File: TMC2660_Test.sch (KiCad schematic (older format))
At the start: 50 parts, among them P101 CONN_4, P102 CONN_4, P103 CONN_2, P104 CONN_13X2, P105 CONN_4, P106 CONN_4, U101 TMC2660, U102 TMC2660, U103 TMC2660, U104 TMC2660

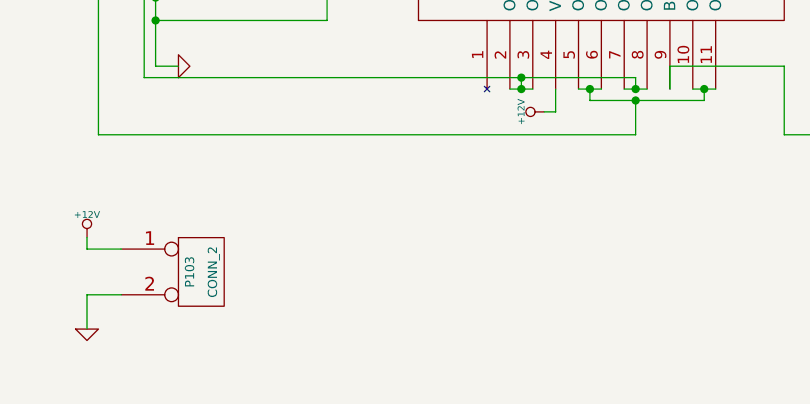
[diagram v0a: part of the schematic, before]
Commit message: Add mounting holes, dummy.
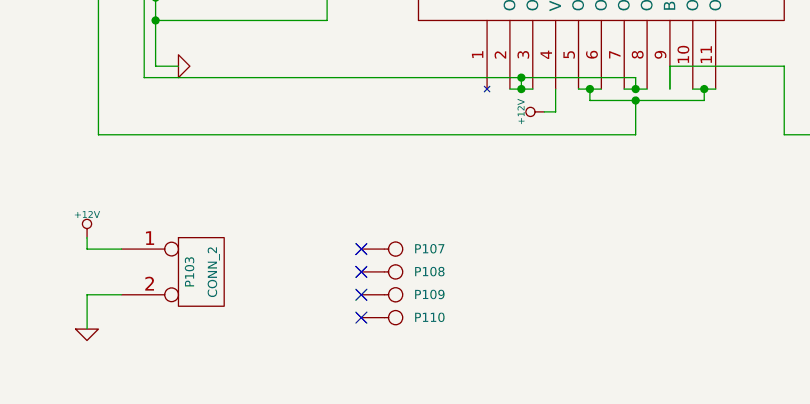
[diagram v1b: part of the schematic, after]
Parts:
- added P107, P108, P109, P110: CONN_1, symbol CONN_1
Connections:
- no-connect marks 8 -> 12
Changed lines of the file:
@@
 $EndComp
 $Comp
-L GND #PWR01
+L GND #PWR103
 U 1 1 53402B12
 P 1500 3100
-F 0 "#PWR01" H 1500 3100 30  0001 C CNN
+F 0 "#PWR103" H 1500 3100 30  0001 C CNN
 F 1 "GND" H 1500 3030 30  0001 C CNN
 F 2 "" H 1500 3100 60  0000 C CNN
@@
 $EndComp
 $Comp
-L VCC #PWR02
+L VCC #PWR107
 U 1 1 53402B23
 P 1750 2200
-F 0 "#PWR02" H 1750 2300 30  0001 C CNN
+F 0 "#PWR107" H 1750 2300 30  0001 C CNN
 F 1 "VCC" H 1750 2300 30  0000 C CNN
 F 2 "" H 1750 2200 60  0000 C CNN
@@
 $EndComp
 $Comp
-L +12V #PWR03
+L +12V #PWR105
 U 1 1 53402B52
 P 1650 1700
-F 0 "#PWR03" H 1650 1650 20  0001 C CNN
+F 0 "#PWR105" H 1650 1650 20  0001 C CNN
 F 1 "+12V" H 1650 1800 30  0000 C CNN
 F 2 "" H 1650 1700 60  0000 C CNN
@@
 X-STEP
 $Comp
-L +12V #PWR04
+L +12V #PWR110
 U 1 1 53402CCE
 P 3100 3300
-F 0 "#PWR04" H 3100 3250 20  0001 C CNN
+F 0 "#PWR110" H 3100 3250 20  0001 C CNN
 F 1 "+12V" H 3100 3400 30  0000 C CNN
 F 2 "" H 3100 3300 60  0000 C CNN
@@
 $EndComp
 $Comp
-L +12V #PWR05
+L +12V #PWR109
 U 1 1 53402EAB
 P 3100 900
-F 0 "#PWR05" H 3100 850 20  0001 C CNN
+F 0 "#PWR109" H 3100 850 20  0001 C CNN
 F 1 "+12V" H 3100 1000 30  0000 C CNN
 F 2 "" H 3100 900 60  0000 C CNN
@@
 	4450 1900 4600 1900
 $Comp
-L GND #PWR06
+L GND #PWR113
 U 1 1 5340331C
 P 5350 2300
-F 0 "#PWR06" H 5350 2300 30  0001 C CNN
+F 0 "#PWR113" H 5350 2300 30  0001 C CNN
 F 1 "GND" H 5350 2230 30  0001 C CNN
 F 2 "" H 5350 2300 60  0000 C CNN
@@
 $EndComp
 $Comp
-L GND #PWR07
+L GND #PWR104
 U 1 1 5340488D
 P 1500 6200
-F 0 "#PWR07" H 1500 6200 30  0001 C CNN
+F 0 "#PWR104" H 1500 6200 30  0001 C CNN
 F 1 "GND" H 1500 6130 30  0001 C CNN
 F 2 "" H 1500 6200 60  0000 C CNN
@@
 $EndComp
 $Comp
-L VCC #PWR08
+L VCC #PWR108
 U 1 1 53404893
 P 1750 5300
-F 0 "#PWR08" H 1750 5400 30  0001 C CNN
+F 0 "#PWR108" H 1750 5400 30  0001 C CNN
 F 1 "VCC" H 1750 5400 30  0000 C CNN
 F 2 "" H 1750 5300 60  0000 C CNN
@@
 $EndComp
 $Comp
-L +12V #PWR09
+L +12V #PWR106
 U 1 1 53404899
 P 1650 4800
-F 0 "#PWR09" H 1650 4750 20  0001 C CNN
+F 0 "#PWR106" H 1650 4750 20  0001 C CNN
 F 1 "+12V" H 1650 4900 30  0000 C CNN
 F 2 "" H 1650 4800 60  0000 C CNN
@@
 Z-STEP
 $Comp
-L +12V #PWR010
+L +12V #PWR112
 U 1 1 534048B5
 P 3100 6400
-F 0 "#PWR010" H 3100 6350 20  0001 C CNN
+F 0 "#PWR112" H 3100 6350 20  0001 C CNN
 F 1 "+12V" H 3100 6500 30  0000 C CNN
 F 2 "" H 3100 6400 60  0000 C CNN
@@
 $EndComp
 $Comp
-L +12V #PWR011
+L +12V #PWR111
 U 1 1 534048BB
 P 3100 4000
-F 0 "#PWR011" H 3100 3950 20  0001 C CNN
+F 0 "#PWR111" H 3100 3950 20  0001 C CNN
 F 1 "+12V" H 3100 4100 30  0000 C CNN
 F 2 "" H 3100 4000 60  0000 C CNN
@@
 	4450 5000 4600 5000
 $Comp
-L GND #PWR012
+L GND #PWR114
 U 1 1 53404906
 P 5350 5400
-F 0 "#PWR012" H 5350 5400 30  0001 C CNN
+F 0 "#PWR114" H 5350 5400 30  0001 C CNN
 F 1 "GND" H 5350 5330 30  0001 C CNN
 F 2 "" H 5350 5400 60  0000 C CNN
@@
 $EndComp
 $Comp
-L GND #PWR013
+L GND #PWR117
 U 1 1 53404974
 P 6950 3100
-F 0 "#PWR013" H 6950 3100 30  0001 C CNN
+F 0 "#PWR117" H 6950 3100 30  0001 C CNN
 F 1 "GND" H 6950 3030 30  0001 C CNN
 F 2 "" H 6950 3100 60  0000 C CNN
@@
 $EndComp
 $Comp
-L VCC #PWR014
+L VCC #PWR120
 U 1 1 5340497A
 P 7200 2200
-F 0 "#PWR014" H 7200 2300 30  0001 C CNN
+F 0 "#PWR120" H 7200 2300 30  0001 C CNN
 F 1 "VCC" H 7200 2300 30  0000 C CNN
 F 2 "" H 7200 2200 60  0000 C CNN
@@
 $EndComp
 $Comp
-L +12V #PWR015
+L +12V #PWR118
 U 1 1 53404980
 P 7100 1700
-F 0 "#PWR015" H 7100 1650 20  0001 C CNN
+F 0 "#PWR118" H 7100 1650 20  0001 C CNN
 F 1 "+12V" H 7100 1800 30  0000 C CNN
 F 2 "" H 7100 1700 60  0000 C CNN
@@
 Y-STEP
 $Comp
-L +12V #PWR016
+L +12V #PWR124
 U 1 1 5340499C
 P 8550 3300
-F 0 "#PWR016" H 8550 3250 20  0001 C CNN
+F 0 "#PWR124" H 8550 3250 20  0001 C CNN
 F 1 "+12V" H 8550 3400 30  0000 C CNN
 F 2 "" H 8550 3300 60  0000 C CNN
@@
 $EndComp
 $Comp
-L +12V #PWR017
+L +12V #PWR123
 U 1 1 534049A2
 P 8550 900
-F 0 "#PWR017" H 8550 850 20  0001 C CNN
+F 0 "#PWR123" H 8550 850 20  0001 C CNN
 F 1 "+12V" H 8550 1000 30  0000 C CNN
 F 2 "" H 8550 900 60  0000 C CNN
@@
 	9900 1900 10050 1900
 $Comp
-L GND #PWR018
+L GND #PWR127
 U 1 1 534049ED
 P 10800 2300
-F 0 "#PWR018" H 10800 2300 30  0001 C CNN
+F 0 "#PWR127" H 10800 2300 30  0001 C CNN
 F 1 "GND" H 10800 2230 30  0001 C CNN
 F 2 "" H 10800 2300 60  0000 C CNN
@@
 $EndComp
 $Comp
-L GND #PWR019
+L GND #PWR119
 U 1 1 53404A5B
 P 7100 6200
-F 0 "#PWR019" H 7100 6200 30  0001 C CNN
+F 0 "#PWR119" H 7100 6200 30  0001 C CNN
 F 1 "GND" H 7100 6130 30  0001 C CNN
 F 2 "" H 7100 6200 60  0000 C CNN
@@
 $EndComp
 $Comp
-L VCC #PWR020
+L VCC #PWR122
 U 1 1 53404A61
 P 7350 5300
-F 0 "#PWR020" H 7350 5400 30  0001 C CNN
+F 0 "#PWR122" H 7350 5400 30  0001 C CNN
 F 1 "VCC" H 7350 5400 30  0000 C CNN
 F 2 "" H 7350 5300 60  0000 C CNN
@@
 $EndComp
 $Comp
-L +12V #PWR021
+L +12V #PWR121
 U 1 1 53404A67
 P 7250 4800
-F 0 "#PWR021" H 7250 4750 20  0001 C CNN
+F 0 "#PWR121" H 7250 4750 20  0001 C CNN
 F 1 "+12V" H 7250 4900 30  0000 C CNN
 F 2 "" H 7250 4800 60  0000 C CNN
@@
 E-STEP
 $Comp
-L +12V #PWR022
+L +12V #PWR126
 U 1 1 53404A83
 P 8700 6400
-F 0 "#PWR022" H 8700 6350 20  0001 C CNN
+F 0 "#PWR126" H 8700 6350 20  0001 C CNN
 F 1 "+12V" H 8700 6500 30  0000 C CNN
 F 2 "" H 8700 6400 60  0000 C CNN
@@
 $EndComp
 $Comp
-L +12V #PWR023
+L +12V #PWR125
 U 1 1 53404A89
 P 8700 4000
-F 0 "#PWR023" H 8700 3950 20  0001 C CNN
+F 0 "#PWR125" H 8700 3950 20  0001 C CNN
 F 1 "+12V" H 8700 4100 30  0000 C CNN
 F 2 "" H 8700 4000 60  0000 C CNN
@@
 	10050 5000 10200 5000
 $Comp
-L GND #PWR024
+L GND #PWR128
 U 1 1 53404AD4
 P 10950 5400
-F 0 "#PWR024" H 10950 5400 30  0001 C CNN
+F 0 "#PWR128" H 10950 5400 30  0001 C CNN
 F 1 "GND" H 10950 5330 30  0001 C CNN
 F 2 "" H 10950 5400 60  0000 C CNN
@@
 $EndComp
 $Comp
-L +12V #PWR025
+L +12V #PWR101
 U 1 1 53404C7D
 P 1100 6950
-F 0 "#PWR025" H 1100 6900 20  0001 C CNN
+F 0 "#PWR101" H 1100 6900 20  0001 C CNN
 F 1 "+12V" H 1100 7050 30  0000 C CNN
 F 2 "" H 1100 6950 60  0000 C CNN
@@
 $EndComp
 $Comp
-L GND #PWR026
+L GND #PWR102
 U 1 1 53404C8C
 P 1100 7350
-F 0 "#PWR026" H 1100 7350 30  0001 C CNN
+F 0 "#PWR102" H 1100 7350 30  0001 C CNN
 F 1 "GND" H 1100 7280 30  0001 C CNN
 F 2 "" H 1100 7350 60  0000 C CNN
@@
 	1100 7000 1250 7000
 $Comp
-L VCC #PWR027
+L VCC #PWR115
 U 1 1 5340502F
 P 5500 5800
-F 0 "#PWR027" H 5500 5900 30  0001 C CNN
+F 0 "#PWR115" H 5500 5900 30  0001 C CNN
 F 1 "VCC" H 5500 5900 30  0000 C CNN
 F 2 "" H 5500 5800 60  0000 C CNN
@@
 $EndComp
 $Comp
-L GND #PWR028
+L GND #PWR116
 U 1 1 5340503E
 P 5950 7550
-F 0 "#PWR028" H 5950 7550 30  0001 C CNN
+F 0 "#PWR116" H 5950 7550 30  0001 C CNN
 F 1 "GND" H 5950 7480 30  0001 C CNN
 F 2 "" H 5950 7550 60  0000 C CNN
@@
 Wire Wire Line
 	1150 800  1150 1950
+$Comp
+L CONN_1 P107
+U 1 1 53442419
+P 2450 7000
+F 0 "P107" H 2530 7000 40  0000 L CNN
+F 1 "CONN_1" H 2450 7055 30  0001 C CNN
+F 2 "" H 2450 7000 60  0000 C CNN
+F 3 "" H 2450 7000 60  0000 C CNN
+	1    2450 7000
+	1    0    0    -1
+$EndComp
+$Comp
+L CONN_1 P108
+U 1 1 53442428
+P 2450 7100
+F 0 "P108" H 2530 7100 40  0000 L CNN
+F 1 "CONN_1" H 2450 7155 30  0001 C CNN
+F 2 "" H 2450 7100 60  0000 C CNN
+F 3 "" H 2450 7100 60  0000 C CNN
+	1    2450 7100
+	1    0    0    -1
+$EndComp
+$Comp
+L CONN_1 P109
+U 1 1 53442437
+P 2450 7200
+F 0 "P109" H 2530 7200 40  0000 L CNN
+F 1 "CONN_1" H 2450 7255 30  0001 C CNN
+F 2 "" H 2450 7200 60  0000 C CNN
+F 3 "" H 2450 7200 60  0000 C CNN
+	1    2450 7200
+	1    0    0    -1
+$EndComp
+$Comp
+L CONN_1 P110
+U 1 1 53442446
+P 2450 7300
+F 0 "P110" H 2530 7300 40  0000 L CNN
+F 1 "CONN_1" H 2450 7355 30  0001 C CNN
+F 2 "" H 2450 7300 60  0000 C CNN
+F 3 "" H 2450 7300 60  0000 C CNN
+	1    2450 7300
+	1    0    0    -1
+$EndComp
+NoConn ~ 2300 7000
+NoConn ~ 2300 7100
+NoConn ~ 2300 7200
+NoConn ~ 2300 7300
 $EndSCHEMATC

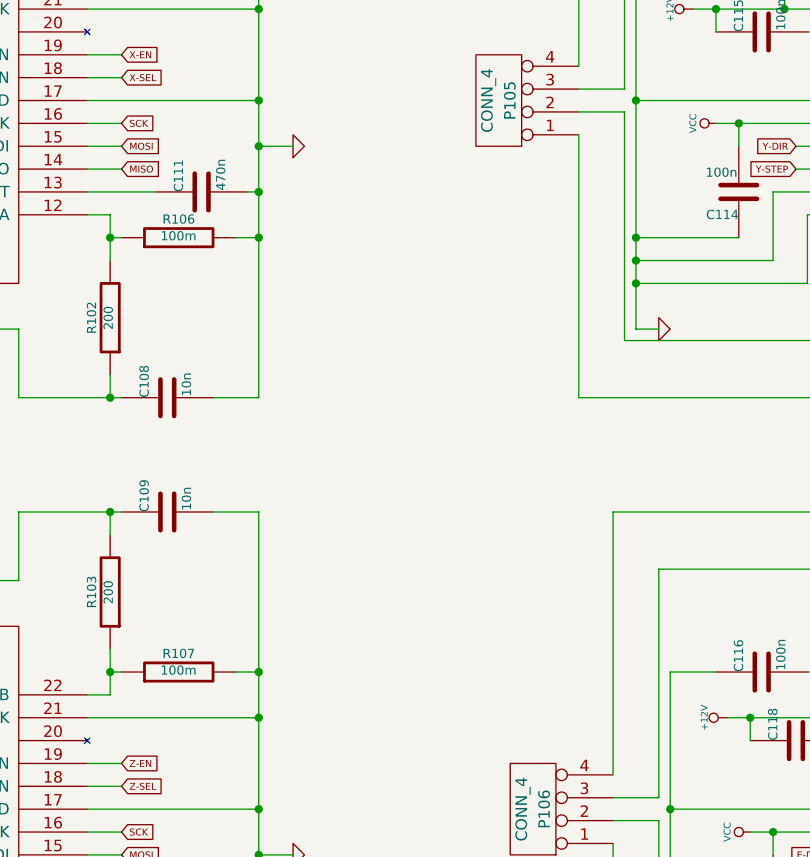
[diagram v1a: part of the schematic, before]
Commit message: Add decoupling caps--one ceramic and one electrolytic per driver.
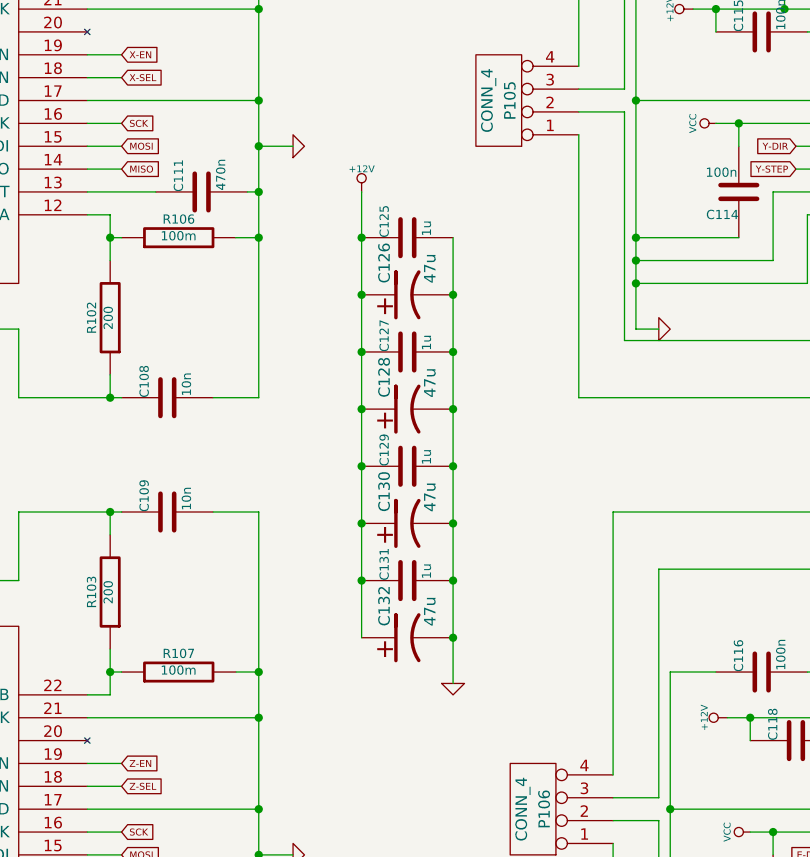
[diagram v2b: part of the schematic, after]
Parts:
- added C125, C127, C129, C131: 1u, symbol C
- added C126, C128, C130, C132: 47u, symbol CP1
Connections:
- net +12V: now also C125.1, C126.1, C127.1, C128.1, C129.1, C130.1, C131.1, C132.1
- net GND: now also C125.2, C126.2, C127.2, C128.2, C129.2, C130.2, C131.2, C132.2
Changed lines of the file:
@@
 $EndComp
 $Comp
-L GND #PWR103
+L GND #PWR01
 U 1 1 53402B12
 P 1500 3100
-F 0 "#PWR103" H 1500 3100 30  0001 C CNN
+F 0 "#PWR01" H 1500 3100 30  0001 C CNN
 F 1 "GND" H 1500 3030 30  0001 C CNN
 F 2 "" H 1500 3100 60  0000 C CNN
@@
 $EndComp
 $Comp
-L VCC #PWR107
+L VCC #PWR02
 U 1 1 53402B23
 P 1750 2200
-F 0 "#PWR107" H 1750 2300 30  0001 C CNN
+F 0 "#PWR02" H 1750 2300 30  0001 C CNN
 F 1 "VCC" H 1750 2300 30  0000 C CNN
 F 2 "" H 1750 2200 60  0000 C CNN
@@
 $EndComp
 $Comp
-L +12V #PWR105
+L +12V #PWR03
 U 1 1 53402B52
 P 1650 1700
-F 0 "#PWR105" H 1650 1650 20  0001 C CNN
+F 0 "#PWR03" H 1650 1650 20  0001 C CNN
 F 1 "+12V" H 1650 1800 30  0000 C CNN
 F 2 "" H 1650 1700 60  0000 C CNN
@@
 X-STEP
 $Comp
-L +12V #PWR110
+L +12V #PWR04
 U 1 1 53402CCE
 P 3100 3300
-F 0 "#PWR110" H 3100 3250 20  0001 C CNN
+F 0 "#PWR04" H 3100 3250 20  0001 C CNN
 F 1 "+12V" H 3100 3400 30  0000 C CNN
 F 2 "" H 3100 3300 60  0000 C CNN
@@
 $EndComp
 $Comp
-L +12V #PWR109
+L +12V #PWR05
 U 1 1 53402EAB
 P 3100 900
-F 0 "#PWR109" H 3100 850 20  0001 C CNN
+F 0 "#PWR05" H 3100 850 20  0001 C CNN
 F 1 "+12V" H 3100 1000 30  0000 C CNN
 F 2 "" H 3100 900 60  0000 C CNN
@@
 	4450 1900 4600 1900
 $Comp
-L GND #PWR113
+L GND #PWR06
 U 1 1 5340331C
 P 5350 2300
-F 0 "#PWR113" H 5350 2300 30  0001 C CNN
+F 0 "#PWR06" H 5350 2300 30  0001 C CNN
 F 1 "GND" H 5350 2230 30  0001 C CNN
 F 2 "" H 5350 2300 60  0000 C CNN
@@
 $EndComp
 $Comp
-L GND #PWR104
+L GND #PWR07
 U 1 1 5340488D
 P 1500 6200
-F 0 "#PWR104" H 1500 6200 30  0001 C CNN
+F 0 "#PWR07" H 1500 6200 30  0001 C CNN
 F 1 "GND" H 1500 6130 30  0001 C CNN
 F 2 "" H 1500 6200 60  0000 C CNN
@@
 $EndComp
 $Comp
-L VCC #PWR108
+L VCC #PWR08
 U 1 1 53404893
 P 1750 5300
-F 0 "#PWR108" H 1750 5400 30  0001 C CNN
+F 0 "#PWR08" H 1750 5400 30  0001 C CNN
 F 1 "VCC" H 1750 5400 30  0000 C CNN
 F 2 "" H 1750 5300 60  0000 C CNN
@@
 $EndComp
 $Comp
-L +12V #PWR106
+L +12V #PWR09
 U 1 1 53404899
 P 1650 4800
-F 0 "#PWR106" H 1650 4750 20  0001 C CNN
+F 0 "#PWR09" H 1650 4750 20  0001 C CNN
 F 1 "+12V" H 1650 4900 30  0000 C CNN
 F 2 "" H 1650 4800 60  0000 C CNN
@@
 Z-STEP
 $Comp
-L +12V #PWR112
+L +12V #PWR010
 U 1 1 534048B5
 P 3100 6400
-F 0 "#PWR112" H 3100 6350 20  0001 C CNN
+F 0 "#PWR010" H 3100 6350 20  0001 C CNN
 F 1 "+12V" H 3100 6500 30  0000 C CNN
 F 2 "" H 3100 6400 60  0000 C CNN
@@
 $EndComp
 $Comp
-L +12V #PWR111
+L +12V #PWR011
 U 1 1 534048BB
 P 3100 4000
-F 0 "#PWR111" H 3100 3950 20  0001 C CNN
+F 0 "#PWR011" H 3100 3950 20  0001 C CNN
 F 1 "+12V" H 3100 4100 30  0000 C CNN
 F 2 "" H 3100 4000 60  0000 C CNN
@@
 	4450 5000 4600 5000
 $Comp
-L GND #PWR114
+L GND #PWR012
 U 1 1 53404906
 P 5350 5400
-F 0 "#PWR114" H 5350 5400 30  0001 C CNN
+F 0 "#PWR012" H 5350 5400 30  0001 C CNN
 F 1 "GND" H 5350 5330 30  0001 C CNN
 F 2 "" H 5350 5400 60  0000 C CNN
@@
 $EndComp
 $Comp
-L GND #PWR117
+L GND #PWR013
 U 1 1 53404974
 P 6950 3100
-F 0 "#PWR117" H 6950 3100 30  0001 C CNN
+F 0 "#PWR013" H 6950 3100 30  0001 C CNN
 F 1 "GND" H 6950 3030 30  0001 C CNN
 F 2 "" H 6950 3100 60  0000 C CNN
@@
 $EndComp
 $Comp
-L VCC #PWR120
+L VCC #PWR014
 U 1 1 5340497A
 P 7200 2200
-F 0 "#PWR120" H 7200 2300 30  0001 C CNN
+F 0 "#PWR014" H 7200 2300 30  0001 C CNN
 F 1 "VCC" H 7200 2300 30  0000 C CNN
 F 2 "" H 7200 2200 60  0000 C CNN
@@
 $EndComp
 $Comp
-L +12V #PWR118
+L +12V #PWR015
 U 1 1 53404980
 P 7100 1700
-F 0 "#PWR118" H 7100 1650 20  0001 C CNN
+F 0 "#PWR015" H 7100 1650 20  0001 C CNN
 F 1 "+12V" H 7100 1800 30  0000 C CNN
 F 2 "" H 7100 1700 60  0000 C CNN
@@
 Y-STEP
 $Comp
-L +12V #PWR124
+L +12V #PWR016
 U 1 1 5340499C
 P 8550 3300
-F 0 "#PWR124" H 8550 3250 20  0001 C CNN
+F 0 "#PWR016" H 8550 3250 20  0001 C CNN
 F 1 "+12V" H 8550 3400 30  0000 C CNN
 F 2 "" H 8550 3300 60  0000 C CNN
@@
 $EndComp
 $Comp
-L +12V #PWR123
+L +12V #PWR017
 U 1 1 534049A2
 P 8550 900
-F 0 "#PWR123" H 8550 850 20  0001 C CNN
+F 0 "#PWR017" H 8550 850 20  0001 C CNN
 F 1 "+12V" H 8550 1000 30  0000 C CNN
 F 2 "" H 8550 900 60  0000 C CNN
@@
 	9900 1900 10050 1900
 $Comp
-L GND #PWR127
+L GND #PWR018
 U 1 1 534049ED
 P 10800 2300
-F 0 "#PWR127" H 10800 2300 30  0001 C CNN
+F 0 "#PWR018" H 10800 2300 30  0001 C CNN
 F 1 "GND" H 10800 2230 30  0001 C CNN
 F 2 "" H 10800 2300 60  0000 C CNN
@@
 $EndComp
 $Comp
-L GND #PWR119
+L GND #PWR019
 U 1 1 53404A5B
 P 7100 6200
-F 0 "#PWR119" H 7100 6200 30  0001 C CNN
+F 0 "#PWR019" H 7100 6200 30  0001 C CNN
 F 1 "GND" H 7100 6130 30  0001 C CNN
 F 2 "" H 7100 6200 60  0000 C CNN
@@
 $EndComp
 $Comp
-L VCC #PWR122
+L VCC #PWR020
 U 1 1 53404A61
 P 7350 5300
-F 0 "#PWR122" H 7350 5400 30  0001 C CNN
+F 0 "#PWR020" H 7350 5400 30  0001 C CNN
 F 1 "VCC" H 7350 5400 30  0000 C CNN
 F 2 "" H 7350 5300 60  0000 C CNN
@@
 $EndComp
 $Comp
-L +12V #PWR121
+L +12V #PWR021
 U 1 1 53404A67
 P 7250 4800
-F 0 "#PWR121" H 7250 4750 20  0001 C CNN
+F 0 "#PWR021" H 7250 4750 20  0001 C CNN
 F 1 "+12V" H 7250 4900 30  0000 C CNN
 F 2 "" H 7250 4800 60  0000 C CNN
@@
 E-STEP
 $Comp
-L +12V #PWR126
+L +12V #PWR022
 U 1 1 53404A83
 P 8700 6400
-F 0 "#PWR126" H 8700 6350 20  0001 C CNN
+F 0 "#PWR022" H 8700 6350 20  0001 C CNN
 F 1 "+12V" H 8700 6500 30  0000 C CNN
 F 2 "" H 8700 6400 60  0000 C CNN
@@
 $EndComp
 $Comp
-L +12V #PWR125
+L +12V #PWR023
 U 1 1 53404A89
 P 8700 4000
-F 0 "#PWR125" H 8700 3950 20  0001 C CNN
+F 0 "#PWR023" H 8700 3950 20  0001 C CNN
 F 1 "+12V" H 8700 4100 30  0000 C CNN
 F 2 "" H 8700 4000 60  0000 C CNN
@@
 	10050 5000 10200 5000
 $Comp
-L GND #PWR128
+L GND #PWR024
 U 1 1 53404AD4
 P 10950 5400
-F 0 "#PWR128" H 10950 5400 30  0001 C CNN
+F 0 "#PWR024" H 10950 5400 30  0001 C CNN
 F 1 "GND" H 10950 5330 30  0001 C CNN
 F 2 "" H 10950 5400 60  0000 C CNN
@@
 $EndComp
 $Comp
-L +12V #PWR101
+L +12V #PWR025
 U 1 1 53404C7D
 P 1100 6950
-F 0 "#PWR101" H 1100 6900 20  0001 C CNN
+F 0 "#PWR025" H 1100 6900 20  0001 C CNN
 F 1 "+12V" H 1100 7050 30  0000 C CNN
 F 2 "" H 1100 6950 60  0000 C CNN
@@
 $EndComp
 $Comp
-L GND #PWR102
+L GND #PWR026
 U 1 1 53404C8C
 P 1100 7350
-F 0 "#PWR102" H 1100 7350 30  0001 C CNN
+F 0 "#PWR026" H 1100 7350 30  0001 C CNN
 F 1 "GND" H 1100 7280 30  0001 C CNN
 F 2 "" H 1100 7350 60  0000 C CNN
@@
 	1100 7000 1250 7000
 $Comp
-L VCC #PWR115
+L VCC #PWR027
 U 1 1 5340502F
 P 5500 5800
-F 0 "#PWR115" H 5500 5900 30  0001 C CNN
+F 0 "#PWR027" H 5500 5900 30  0001 C CNN
 F 1 "VCC" H 5500 5900 30  0000 C CNN
 F 2 "" H 5500 5800 60  0000 C CNN
@@
 $EndComp
 $Comp
-L GND #PWR116
+L GND #PWR028
 U 1 1 5340503E
 P 5950 7550
-F 0 "#PWR116" H 5950 7550 30  0001 C CNN
+F 0 "#PWR028" H 5950 7550 30  0001 C CNN
 F 1 "GND" H 5950 7480 30  0001 C CNN
 F 2 "" H 5950 7550 60  0000 C CNN
@@
 NoConn ~ 2300 7200
 NoConn ~ 2300 7300
+$Comp
+L C C129
+U 1 1 5367C896
+P 5850 3700
+F 0 "C129" H 5850 3800 40  0000 L CNN
+F 1 "1u" H 5856 3615 40  0000 L CNN
+F 2 "" H 5888 3550 30  0000 C CNN
+F 3 "" H 5850 3700 60  0000 C CNN
+	1    5850 3700
+	0    -1   -1   0
+$EndComp
+$Comp
+L CP1 C130
+U 1 1 5367C8B4
+P 5850 3950
+F 0 "C130" H 5900 4050 50  0000 L CNN
+F 1 "47u" H 5900 3850 50  0000 L CNN
+F 2 "" H 5850 3950 60  0000 C CNN
+F 3 "" H 5850 3950 60  0000 C CNN
+	1    5850 3950
+	0    -1   -1   0
+$EndComp
+$Comp
+L C C131
+U 1 1 5367C97C
+P 5850 4200
+F 0 "C131" H 5850 4300 40  0000 L CNN
+F 1 "1u" H 5856 4115 40  0000 L CNN
+F 2 "" H 5888 4050 30  0000 C CNN
+F 3 "" H 5850 4200 60  0000 C CNN
+	1    5850 4200
+	0    -1   -1   0
+$EndComp
+$Comp
+L CP1 C132
+U 1 1 5367C982
+P 5850 4450
+F 0 "C132" H 5900 4550 50  0000 L CNN
+F 1 "47u" H 5900 4350 50  0000 L CNN
+F 2 "" H 5850 4450 60  0000 C CNN
+F 3 "" H 5850 4450 60  0000 C CNN
+	1    5850 4450
+	0    -1   -1   0
+$EndComp
+$Comp
+L C C125
+U 1 1 5367C988
+P 5850 2700
+F 0 "C125" H 5850 2800 40  0000 L CNN
+F 1 "1u" H 5856 2615 40  0000 L CNN
+F 2 "" H 5888 2550 30  0000 C CNN
+F 3 "" H 5850 2700 60  0000 C CNN
+	1    5850 2700
+	0    -1   -1   0
+$EndComp
+$Comp
+L CP1 C126
+U 1 1 5367C98E
+P 5850 2950
+F 0 "C126" H 5900 3050 50  0000 L CNN
+F 1 "47u" H 5900 2850 50  0000 L CNN
+F 2 "" H 5850 2950 60  0000 C CNN
+F 3 "" H 5850 2950 60  0000 C CNN
+	1    5850 2950
+	0    -1   -1   0
+$EndComp
+$Comp
+L C C127
+U 1 1 5367C994
+P 5850 3200
+F 0 "C127" H 5850 3300 40  0000 L CNN
+F 1 "1u" H 5856 3115 40  0000 L CNN
+F 2 "" H 5888 3050 30  0000 C CNN
+F 3 "" H 5850 3200 60  0000 C CNN
+	1    5850 3200
+	0    -1   -1   0
+$EndComp
+$Comp
+L CP1 C128
+U 1 1 5367C99A
+P 5850 3450
+F 0 "C128" H 5900 3550 50  0000 L CNN
+F 1 "47u" H 5900 3350 50  0000 L CNN
+F 2 "" H 5850 3450 60  0000 C CNN
+F 3 "" H 5850 3450 60  0000 C CNN
+	1    5850 3450
+	0    -1   -1   0
+$EndComp
+Wire Wire Line
+	5650 2500 5650 4450
+Connection ~ 5650 2950
+Connection ~ 5650 3200
+Connection ~ 5650 3450
+Connection ~ 5650 3700
+Connection ~ 5650 3950
+Connection ~ 5650 4200
+Wire Wire Line
+	6050 2700 6050 4650
+Connection ~ 6050 4200
+Connection ~ 6050 3950
+Connection ~ 6050 3700
+Connection ~ 6050 3450
+Connection ~ 6050 3200
+Connection ~ 6050 2950
+$Comp
+L +12V #PWR029
+U 1 1 5367E510
+P 5650 2500
+F 0 "#PWR029" H 5650 2450 20  0001 C CNN
+F 1 "+12V" H 5650 2600 30  0000 C CNN
+F 2 "" H 5650 2500 60  0000 C CNN
+F 3 "" H 5650 2500 60  0000 C CNN
+	1    5650 2500
+	1    0    0    -1
+$EndComp
+Connection ~ 5650 2700
+$Comp
+L GND #PWR030
+U 1 1 5367E71C
+P 6050 4650
+F 0 "#PWR030" H 6050 4650 30  0001 C CNN
+F 1 "GND" H 6050 4580 30  0001 C CNN
+F 2 "" H 6050 4650 60  0000 C CNN
+F 3 "" H 6050 4650 60  0000 C CNN
+	1    6050 4650
+	1    0    0    -1
+$EndComp
+Connection ~ 6050 4450
 $EndSCHEMATC

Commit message: Added more capacitors!
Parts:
- added C133, C135, C137, C139: 1u, symbol C
- added C134, C136, C138, C140: 47u, symbol CP1
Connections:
- net +12V: now also C133.1, C134.1, C135.1, C136.1, C137.1, C138.1, C139.1, C140.1
- net GND: now also C133.2, C134.2, C135.2, C136.2, C137.2, C138.2, C139.2, C140.2
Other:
- moved on the sheet: C125, C126, C127, C128, C129, C130, C131, C132
